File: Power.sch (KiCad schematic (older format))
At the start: 33 parts, among them U4 MP4570GF, U5 AP65251, U6 AZ1117-3.3

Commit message: Added Component-Associations (about 10% remaining)
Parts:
- removed R?: 0, symbol Device:R
- added R? (x2): 0, symbol Device:R
- C12, C14, C17: value 0.1μF -> 100nF; Buy (none) -> https://www.digikey.com/product-detail/en/kemet/C0603C104M5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
- C15: Buy (none) -> https://www.digikey.com/product-detail/en/samsung-electro-m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
- C6: Buy (none) -> https://www.digikey.com/product-detail/en/kemet/C0603C223K1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
- C8, C9: value 0.1μF -> 100nF; footprint Capacitors_SMD:C_0603 -> Capacitors_SMD:C_0805; Buy (none) -> https://www.digikey.com/product-detail/en/samsung-electro-m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
- R10, R3, R5, R6: Buy (none) -> https://www.digikey.com/product-detail/en/yageo/RC0603FR-07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
- R4: Buy (none) -> https://www.digikey.com/product-detail/en/yageo/RC0603JR-07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
- R7: value 213 -> 910; Buy (none) -> https://www.digikey.com/product-detail/en/yageo/RC0603FR-07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
- R8: Buy (none) -> https://www.digikey.com/product-detail/en/yageo/RC0603JR-10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
- R9: value 73k3 -> 73k2; Buy (none) -> https://www.digikey.com/product-detail/en/yageo/RC0603FR-07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
- R? (x2): Buy (none) -> https://www.digikey.com/product-detail/en/stackpole-electro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
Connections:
- net +12V: now also R?.1
- net 3V3: now also R?.1
- net at U6.2 (VO): now also R?.2
- net at L1.2, R6.1, R?.2: now also R?.2
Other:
- moved on the sheet: R?
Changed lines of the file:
@@
 U 1 1 5A4D442D
 P 9375 1675
-F 0 "U6" H 9225 1800 50  0000 C CNN
-F 1 "AZ1117-3.3" H 9375 1800 50  0000 L CNN
+F 0 "U6" H 9525 1425 50  0000 C CNN
+F 1 "AZ1117-3.3" H 9150 1800 50  0000 L CNN
 F 2 "TO_SOT_Packages_SMD:SOT-223-3_TabPin2" H 9375 1925 50  0001 C CIN
 F 3 "" H 9375 1675 50  0001 C CNN
@@
 F 2 "Resistors_SMD:R_0603" V 4705 1525 50  0001 C CNN
 F 3 "" H 4775 1525 50  0001 C CNN
+F 4 "https://www.digikey.com/product-detail/en/yageo/RC0603JR-10100KL/YAG2294CT-ND/5252408" V 4775 1525 50  0001 C CNN "Buy"
 	1    4775 1525
 	1    0    0    -1
@@
 P 6425 1825
 F 0 "R9" V 6505 1825 50  0000 C CNN
-F 1 "73k3" V 6425 1825 50  0000 C CNN
+F 1 "73k2" V 6425 1825 50  0000 C CNN
 F 2 "Resistors_SMD:R_0603" V 6355 1825 50  0001 C CNN
 F 3 "" H 6425 1825 50  0001 C CNN
+F 4 "https://www.digikey.com/product-detail/en/yageo/RC0603FR-0773K2L/311-73.2KHRCT-ND/730321" V 6425 1825 50  0001 C CNN "Buy"
 	1    6425 1825
 	1    0    0    -1
@@
 F 2 "Resistors_SMD:R_0603" V 6355 2225 50  0001 C CNN
 F 3 "" H 6425 2225 50  0001 C CNN
+F 4 "https://www.digikey.com/product-detail/en/yageo/RC0603FR-0710KL/311-10.0KHRCT-ND/729827" V 6425 2225 50  0001 C CNN "Buy"
 	1    6425 2225
 	1    0    0    -1
@@
 P 5825 1525
 F 0 "C14" H 5875 1425 50  0000 L CNN
-F 1 "0.1μF" H 5875 1625 50  0000 L CNN
+F 1 "100nF" H 5875 1625 50  0000 L CNN
 F 2 "Capacitors_SMD:C_0603" H 5863 1375 50  0001 C CNN
 F 3 "" H 5825 1525 50  0001 C CNN
+F 4 "https://www.digikey.com/product-detail/en/kemet/C0603C104M5RACTU/399-7845-1-ND/3471568" H 5825 1525 50  0001 C CNN "Buy"
 	1    5825 1525
 	1    0    0    -1
@@
 F 2 "Capacitors_SMD:C_0603" H 6713 1675 50  0001 C CNN
 F 3 "" H 6675 1825 50  0001 C CNN
+F 4 "https://www.digikey.com/product-detail/en/samsung-electro-mechanics/CL10C300JB8NNNC/1276-1021-1-ND/3889107" H 6675 1825 50  0001 C CNN "Buy"
 	1    6675 1825
 	1    0    0    -1
@@
 P 7600 1825
 F 0 "C17" H 7625 1925 50  0000 L CNN
-F 1 "0.1μF" H 7625 1725 50  0000 L CNN
+F 1 "100nF" H 7625 1725 50  0000 L CNN
 F 2 "Capacitors_SMD:C_0603" H 7638 1675 50  0001 C CNN
 F 3 "" H 7600 1825 50  0001 C CNN
+F 4 "https://www.digikey.com/product-detail/en/kemet/C0603C104M5RACTU/399-7845-1-ND/3471568" H 7600 1825 50  0001 C CNN "Buy"
 	1    7600 1825
 	1    0    0    -1
@@
 U 1 1 5A513860
 P 1550 2500
-F 0 "U4" H 1950 3600 60  0000 C CNN
+F 0 "U4" H 1950 2100 60  0000 C CNN
 F 1 "MP4570GF" H 1550 2900 60  0000 C CNN
 F 2 "Housings_SSOP:HTSSOP-20-1EP_4.4x6.5mm_Pitch0.65mm_ThermalPad" H 400 2900 60  0001 C CNN
@@
 P 2150 1750
 F 0 "C9" H 2160 1820 50  0000 L CNN
-F 1 "0.1μF" H 2150 1675 50  0000 L CNN
-F 2 "Capacitors_SMD:C_0603" H 2150 1750 50  0001 C CNN
+F 1 "100nF" H 2150 1675 50  0000 L CNN
+F 2 "Capacitors_SMD:C_0805" H 2150 1750 50  0001 C CNN
 F 3 "" H 2150 1750 50  0001 C CNN
+F 4 "https://www.digikey.com/product-detail/en/samsung-electro-mechanics/CL21B104KCFWPNE/1276-6733-1-ND/5961592" H 2150 1750 50  0001 C CNN "Buy"
 	1    2150 1750
 	1    0    0    -1
@@
 F 2 "Resistors_SMD:R_0603" V 880 2800 50  0001 C CNN
 F 3 "" H 950 2800 50  0001 C CNN
+F 4 "https://www.digikey.com/product-detail/en/yageo/RC0603FR-0773K2L/311-73.2KHRCT-ND/730321" V 950 2800 50  0001 C CNN "Buy"
 	1    950  2800
 	1    0    0    -1
@@
 P 1750 1100
 F 0 "C8" H 1760 1170 50  0000 L CNN
-F 1 "0.1μF" H 1760 1020 50  0000 L CNN
-F 2 "Capacitors_SMD:C_0603" H 1750 1100 50  0001 C CNN
+F 1 "100nF" H 1750 1025 50  0000 L CNN
+F 2 "Capacitors_SMD:C_0805" H 1750 1100 50  0001 C CNN
 F 3 "" H 1750 1100 50  0001 C CNN
+F 4 "https://www.digikey.com/product-detail/en/samsung-electro-mechanics/CL21B104KCFWPNE/1276-6733-1-ND/5961592" H 1750 1100 50  0001 C CNN "Buy"
 	1    1750 1100
 	0    -1   -1   0
@@
 F 2 "Resistors_SMD:R_0603" V 680 1600 50  0001 C CNN
 F 3 "" H 750 1600 50  0001 C CNN
+F 4 "https://www.digikey.com/product-detail/en/yageo/RC0603JR-071ML/311-1.0MGRCT-ND/729625" V 750 1600 50  0001 C CNN "Buy"
 	1    750  1600
 	0    1    1    0
@@
 	0    -1   -1   0
 $EndComp
-Text Notes 2450 1750 0    60   ~ 0
+Text Notes 2350 1675 0    60   ~ 0
 Large enough?
 Wire Wire Line
@@
 F 2 "Resistors_SMD:R_0603" V 2730 2100 50  0001 C CNN
 F 3 "" H 2800 2100 50  0001 C CNN
+F 4 "https://www.digikey.com/product-detail/en/yageo/RC0603FR-0710KL/311-10.0KHRCT-ND/729827" V 2800 2100 50  0001 C CNN "Buy"
 	1    2800 2100
 	1    0    0    -1
@@
 P 2800 2500
 F 0 "R7" V 2880 2500 50  0000 C CNN
-F 1 "213" V 2800 2500 50  0000 C CNN
+F 1 "910" V 2800 2500 50  0000 C CNN
 F 2 "Resistors_SMD:R_0603" V 2730 2500 50  0001 C CNN
 F 3 "" H 2800 2500 50  0001 C CNN
+F 4 "https://www.digikey.com/product-detail/en/yageo/RC0603FR-07909RL/311-909HRCT-ND/730372" V 2800 2500 50  0001 C CNN "Buy"
 	1    2800 2500
 	1    0    0    -1
@@
 P 3850 2100
 F 0 "C12" H 3860 2170 50  0000 L CNN
-F 1 "0.1μF" H 3850 2025 50  0000 L CNN
+F 1 "100nF" H 3850 2025 50  0000 L CNN
 F 2 "Capacitors_SMD:C_0603" H 3850 2100 50  0001 C CNN
 F 3 "" H 3850 2100 50  0001 C CNN
+F 4 "https://www.digikey.com/product-detail/en/kemet/C0603C104M5RACTU/399-7845-1-ND/3471568" H 3850 2100 50  0001 C CNN "Buy"
 	1    3850 2100
 	1    0    0    -1
@@
 F 2 "Resistors_SMD:R_0603" V 630 2600 50  0001 C CNN
 F 3 "" H 700 2600 50  0001 C CNN
+F 4 "https://www.digikey.com/product-detail/en/yageo/RC0603FR-0730K9L/311-30.9KHRCT-ND/730091" V 700 2600 50  0001 C CNN "Buy"
 	1    700  2600
 	1    0    0    -1
@@
 F 2 "Capacitors_SMD:C_0603" H 700 2900 50  0001 C CNN
 F 3 "" H 700 2900 50  0001 C CNN
+F 4 "https://www.digikey.com/product-detail/en/kemet/C0603C223K1RACTU/399-3476-1-ND/754769" H 700 2900 50  0001 C CNN "Buy"
 	1    700  2900
 	1    0    0    -1
@@
 Wire Wire Line
 	700  3050 700  3000
-Text Notes 2200 2050 0    60   ~ 0
+Text Notes 2175 2050 0    60   ~ 0
 Ipk >= 3.3A
 Text Notes 2650 1850 0    60   ~ 0
@@
 	1    0    0    -1
 $EndComp
-$Comp
-L Device:R R?
-U 1 1 5AB66B3A
-P 9900 1675
-F 0 "R?" V 9825 1675 50  0000 C CNN
-F 1 "0" V 9900 1675 50  0000 C CNN
-F 2 "" V 9830 1675 50  0001 C CNN
-F 3 "~" H 9900 1675 50  0001 C CNN
-	1    9900 1675
-	0    1    1    0
-$EndComp
 Wire Wire Line
 	9675 1675 9750 1675
@@
 F 2 "" V 6880 1675 50  0001 C CNN
 F 3 "~" H 6950 1675 50  0001 C CNN
+F 4 "https://www.digikey.com/product-detail/en/stackpole-electronics-inc/RMCF1206ZG0R00/RMCF1206ZG0R00CT-ND/4425382" V 6950 1675 50  0001 C CNN "Buy"
 	1    6950 1675
 	0    1    1    0
@@
 L Device:R R?
 U 1 1 5AB8CA9D
-P 3025 1900
-F 0 "R?" V 2950 1900 50  0000 C CNN
-F 1 "0" V 3025 1900 50  0000 C CNN
-F 2 "" V 2955 1900 50  0001 C CNN
-F 3 "~" H 3025 1900 50  0001 C CNN
-	1    3025 1900
+P 3025 1800
+F 0 "R?" V 2950 1800 50  0000 C CNN
+F 1 "0" V 3025 1800 50  0000 C CNN
+F 2 "" V 2955 1800 50  0001 C CNN
+F 3 "~" H 3025 1800 50  0001 C CNN
+F 4 "https://www.digikey.com/product-detail/en/stackpole-electronics-inc/RMCF1206ZG0R00/RMCF1206ZG0R00CT-ND/4425382" V 3025 1800 50  0001 C CNN "Buy"
+	1    3025 1800
 	0    1    1    0
 $EndComp
@@
 Connection ~ 3250 1900
 Connection ~ 3350 1900
+$Comp
+L Device:R R?
+U 1 1 5AB21F05
+P 3025 1975
+F 0 "R?" V 2950 1975 50  0000 C CNN
+F 1 "0" V 3025 1975 50  0000 C CNN
+F 2 "" V 2955 1975 50  0001 C CNN
+F 3 "~" H 3025 1975 50  0001 C CNN
+F 4 "https://www.digikey.com/product-detail/en/stackpole-electronics-inc/RMCF1206ZG0R00/RMCF1206ZG0R00CT-ND/4425382" V 3025 1975 50  0001 C CNN "Buy"
+	1    3025 1975
+	0    1    1    0
+$EndComp
+Wire Wire Line
+	2875 1975 2875 1900
+Wire Wire Line
+	2875 1900 2875 1800
+Connection ~ 2875 1900
+Wire Wire Line
+	3175 1800 3175 1900
+Connection ~ 3175 1900
+Wire Wire Line
+	3175 1900 3175 1975
+$Comp
+L Device:R R?
+U 1 1 5AB36C51
+P 9900 1675
+F 0 "R?" V 9825 1675 50  0000 C CNN
+F 1 "0" V 9900 1675 50  0000 C CNN
+F 2 "" V 9830 1675 50  0001 C CNN
+F 3 "~" H 9900 1675 50  0001 C CNN
+F 4 "https://www.digikey.com/product-detail/en/stackpole-electronics-inc/RMCF1206ZG0R00/RMCF1206ZG0R00CT-ND/4425382" V 9900 1675 50  0001 C CNN "Buy"
+	1    9900 1675
+	0    1    1    0
+$EndComp
 $EndSCHEMATC

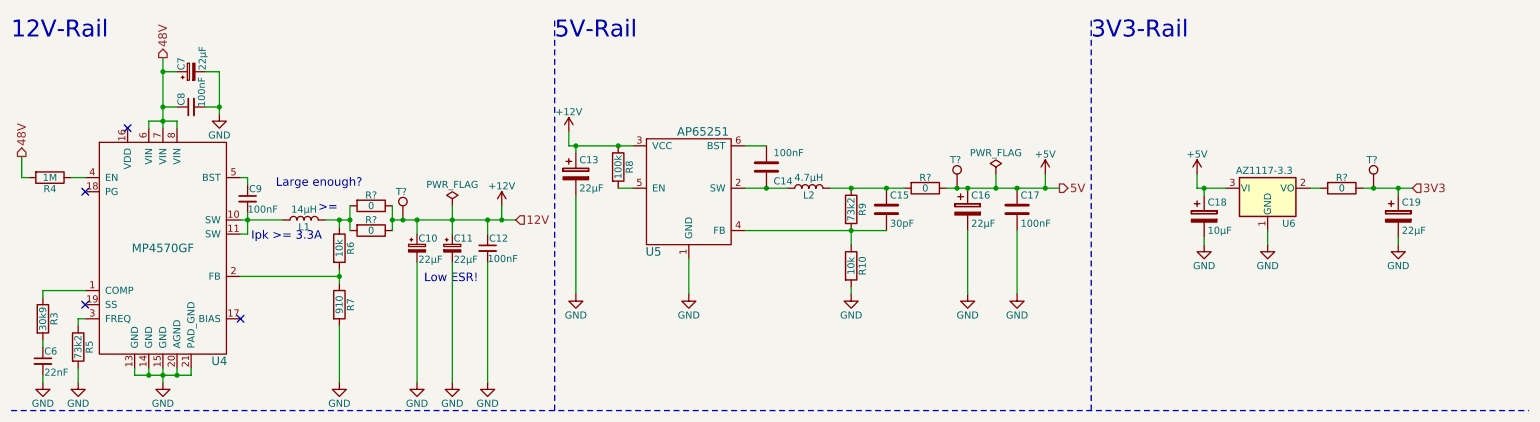
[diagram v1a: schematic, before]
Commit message: Minor changes to layout and component association
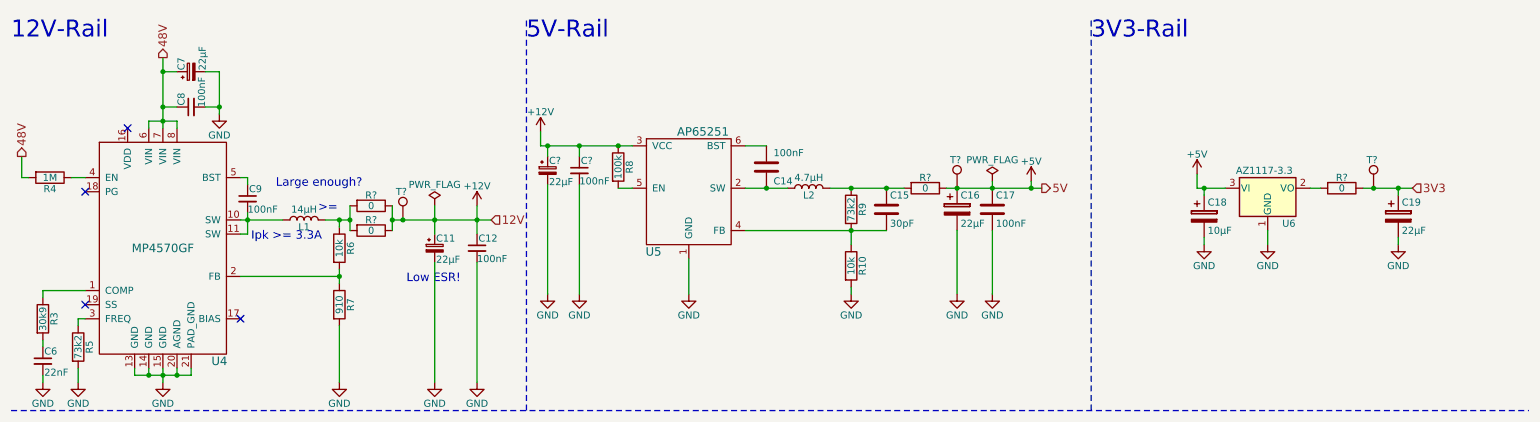
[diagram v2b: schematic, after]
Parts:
- removed C10: 22μF, Capacitors_SMD:C_0603, symbol Device:CP_Small
- removed C13: 22μF, Capacitors_SMD:C_0603, symbol Device:CP
- added C?: 100nF, Capacitors_SMD:C_0603, symbol Device:C_Small
- added C?: 22μF, Capacitors_SMD:C_0603, symbol Device:CP_Small
- C12, C14, C17: Buy https://www.digikey.com/product-detail/en/kemet/C0603C104M5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 -> https://www.digikey.com/product-detail/en/kemet/C0603C104K3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
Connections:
- net +12V: now also C?.1, C?.1
- net GND: now also C?.2, C?.2
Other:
- moved on the sheet: C11, C12, C16, C17

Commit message: Added a missing cap
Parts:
- added C?: 1μF, symbol Device:CP_Small
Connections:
- net GND: now also C?.2
- net at U4.16 (VDD): now also C?.1
- no-connect marks 4 -> 3
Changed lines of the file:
@@
 Text HLabel 7775 1675 2    60   Output ~ 0
 5V
-$Comp
-L switchingR:MP4570GF U4
-U 1 1 5A513860
-P 1550 2500
-F 0 "U4" H 1950 2100 60  0000 C CNN
-F 1 "MP4570GF" H 1550 2900 60  0000 C CNN
-F 2 "Housings_SSOP:HTSSOP-20-1EP_4.4x6.5mm_Pitch0.65mm_ThermalPad" H 400 2900 60  0001 C CNN
-F 3 "" H 400 2900 60  0001 C CNN
-	1    1550 2500
-	1    0    0    -1
-$EndComp
 Text HLabel 1550 750  1    60   Output ~ 0
 48V
@@
 $EndComp
 NoConn ~ 1000 1700
-NoConn ~ 1300 1250
 $Comp
 L Device:R R4
@@
 Wire Wire Line
 	7700 1675 7775 1675
+$Comp
+L switchingR:MP4570GF U4
+U 1 1 5A513860
+P 1550 2500
+F 0 "U4" H 1950 2100 60  0000 C CNN
+F 1 "MP4570GF" H 1550 2900 60  0000 C CNN
+F 2 "Housings_SSOP:HTSSOP-20-1EP_4.4x6.5mm_Pitch0.65mm_ThermalPad" H 400 2900 60  0001 C CNN
+F 3 "" H 400 2900 60  0001 C CNN
+	1    1550 2500
+	1    0    0    -1
+$EndComp
+$Comp
+L Device:CP_Small C?
+U 1 1 5AC62BA2
+P 1100 1100
+F 0 "C?" H 1225 1100 50  0000 C CNN
+F 1 "1μF" H 950 1100 50  0000 C CNN
+F 2 "" H 1100 1100 50  0001 C CNN
+F 3 "~" H 1100 1100 50  0001 C CNN
+	1    1100 1100
+	0    1    1    0
+$EndComp
+$Comp
+L power:GND #PWR?
+U 1 1 5AC694B3
+P 900 1150
+F 0 "#PWR?" H 900 900 50  0001 C CNN
+F 1 "GND" H 900 1000 50  0000 C CNN
+F 2 "" H 900 1150 50  0001 C CNN
+F 3 "" H 900 1150 50  0001 C CNN
+	1    900  1150
+	1    0    0    -1
+$EndComp
+Wire Wire Line
+	900  1150 900  1100
+Wire Wire Line
+	900  1100 1000 1100
+Wire Wire Line
+	1200 1100 1300 1100
+Wire Wire Line
+	1300 1100 1300 1250
 $EndSCHEMATC

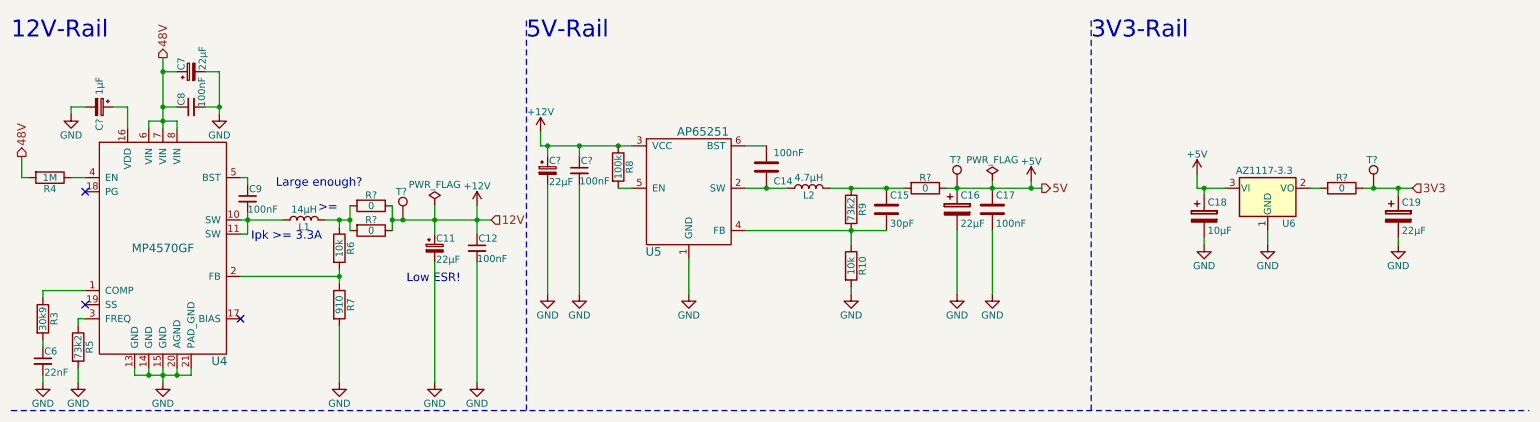
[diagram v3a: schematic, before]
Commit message: Added about 8% of the remaining components
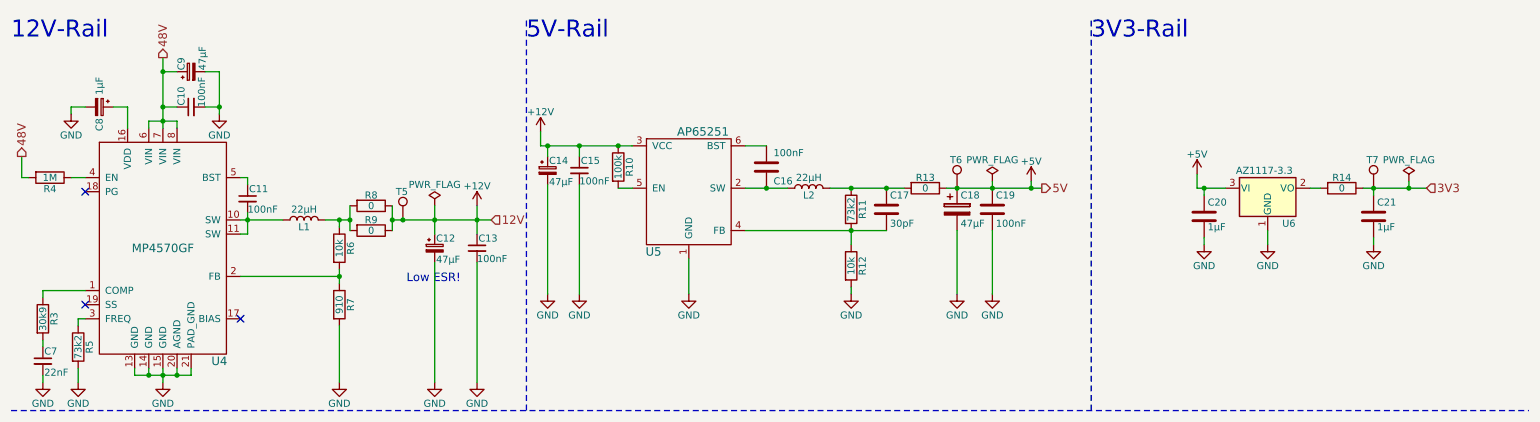
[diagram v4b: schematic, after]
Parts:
- removed C18: 10μF, Capacitors_SMD:C_0603, symbol Device:CP
- removed C19: 22μF, Capacitors_SMD:C_0603, symbol Device:CP
- added C20, C21: 1μF, symbol Device:C
- C12: renamed from C11; value 22μF -> 47μF; footprint Capacitors_SMD:C_0603 -> (none); Buy (none) -> https://www.digikey.com/product-detail/en/rubycon/25TXV47M6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
- C14: renamed from C?; value 22μF -> 47μF; footprint Capacitors_SMD:C_0603 -> (none); Buy (none) -> https://www.digikey.com/product-detail/en/rubycon/25TXV47M6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
- C18: renamed from C16; value 22μF -> 47μF; footprint Capacitors_SMD:C_0603 -> (none); Buy (none) -> https://www.digikey.com/product-detail/en/rubycon/25TXV47M6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
- C8: renamed from C?; Buy (none) -> https://www.digikey.com/product-detail/en/tdk-corporation/C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
- C9: renamed from C7; value 22μF -> 47μF; footprint Capacitors_SMD:C_0603 -> (none); Buy (none) -> https://www.digikey.com/product-detail/en/panasonic-electro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
- L1: value 14μH -> 22μH; Buy (none) -> https://www.digikey.com/product-detail/en/bourns-inc/SRR120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
- L2: value 4.7μH -> 22μH; Buy (none) -> https://www.digikey.com/product-detail/en/taiyo-yuden/NR804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
- U4: Buy (none) -> https://www.mouser.de/ProductDetail/Monolithic-Power-System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
- U6: Buy (none) -> https://www.digikey.com/product-detail/en/diodes-incorporat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
- gave numbers to parts that had none: 8
- renumbered C8 to C10, C9 to C11, C12 to C13, C14 to C16, C15 to C17, C17 to C19, C6 to C7, R8 to R10, R9 to R11, R10 to R12
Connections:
- net +5V: now also C20.1
- net 3V3: now also C21.1
- net GND: now also C20.2, C21.2
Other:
- note removed: ">="
- note removed: "Ipk >= 3.3A"
- note removed: "Large enough?"

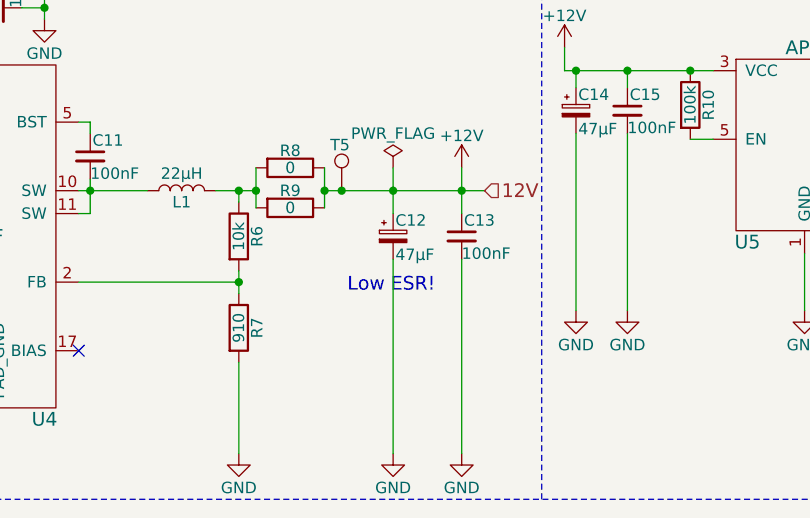
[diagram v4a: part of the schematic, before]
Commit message: Added Gate Pull-Downs
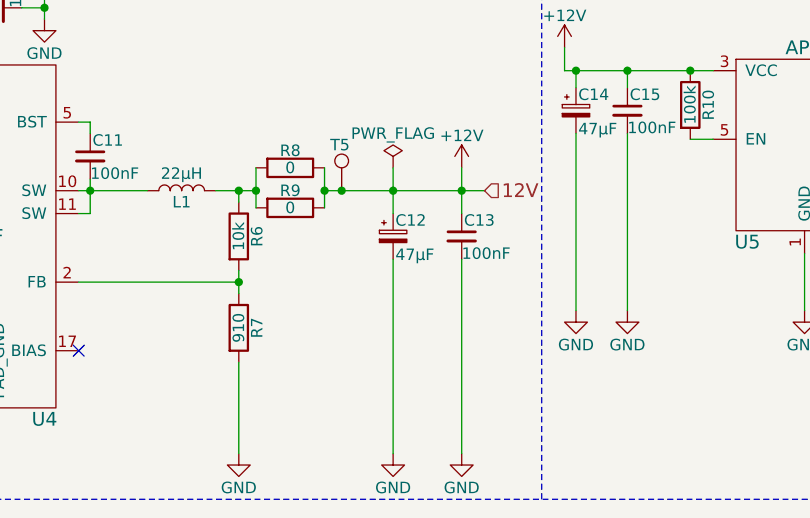
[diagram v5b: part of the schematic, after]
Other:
- note removed: "Low ESR!"
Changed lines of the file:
@@
 	1    0    0    -1
 $EndComp
-Text Notes 3275 2350 0    60   ~ 0
-Low ESR!
 $Comp
 L Device:R R3
